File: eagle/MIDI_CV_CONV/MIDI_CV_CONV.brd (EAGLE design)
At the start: 94 x 71.1 mm, 37 parts, among them CN1 PWR9V, IC1 MCP4922, IC2 TLP552, IC3 74HC541N, IC4 TD62003

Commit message: Finish Soldering
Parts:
- moved R5 18.0 mm to (66.0, 63.5)
- moved R6 10.2 mm to (57.1, 66.0)
- moved JP1 5.39 mm to (8.89, 43.2), turned to 0 degrees
- moved C4 5.08 mm to (66.0, 11.4)
- moved CN1 2.54 mm to (36.8, 63.5)
- moved JP8 2.54 mm to (26.7, 38.1)
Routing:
- net +5V: track 290.4 -> 240.4 mm, vias 0 -> 2
- net N$26: track 46.3 -> 27.5 mm
- net N$1: track 12.7 -> 10.2 mm
- net N$2: track 53.3 -> 55.9 mm
- net +9V: track 10.2 -> 7.62 mm
- net N$24: track 3.61 -> 5.09 mm
- net N$3: track 17.3 -> 16.3 mm
- net GND: vias 2 -> 0

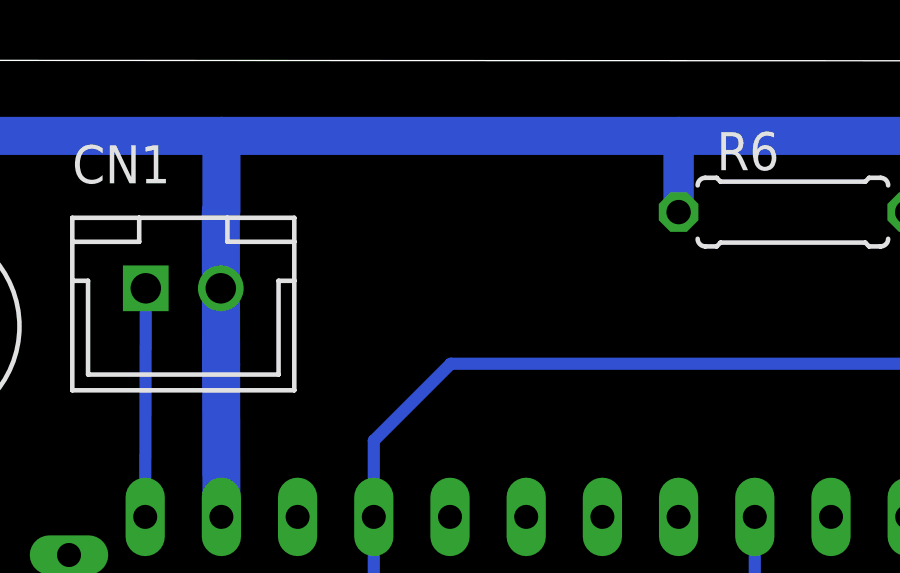
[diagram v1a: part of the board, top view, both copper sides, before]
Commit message: Add: 5V Power Supply
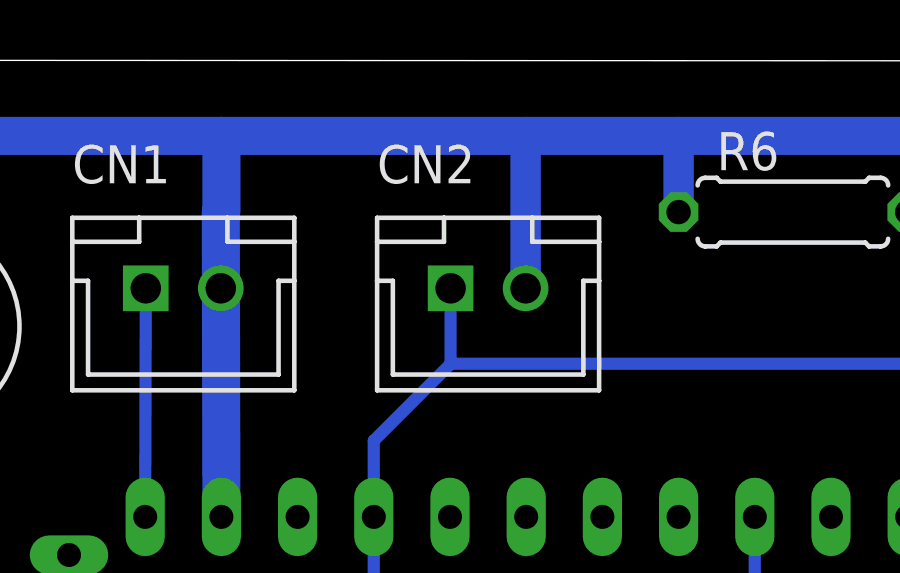
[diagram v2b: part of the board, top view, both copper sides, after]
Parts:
- added CN2: PWR5V, jst-xh:B2B-XH-A
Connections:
- net +5V: now also CN2.1
- net GND: now also CN2.2
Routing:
- net GND: track 298.4 -> 303.5 mm
- net +5V: track 240.4 -> 243.0 mm
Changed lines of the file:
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@@
 <element name="U$1" library="Arduino-clone" package="PRO-MINI-2" value="PRO-MINI-2 (16MHz/5V)" x="48.26" y="49.53" rot="R90"/>
 <element name="JP6" library="pinhead" library_urn="urn:adsk.eagle:library:325" package="1X01" package3d_urn="urn:adsk.eagle:package:22485/2" value="TP_CHK" x="68.58" y="43.18"/>
+<element name="CN2" library="jst-xh" package="B2B-XH-A" value="PWR5V" x="46.99" y="63.5"/>
 </elements>
 <signals>
@@
 <wire x1="10.16" y1="60.96" x2="5.08" y2="55.88" width="0.4064" layer="16"/>
 <wire x1="27.94" y1="60.96" x2="27.94" y2="53.34" width="0.4064" layer="16"/>
+<contactref element="CN2" pad="1"/>
+<wire x1="45.74" y1="63.5" x2="45.74" y2="60.9908" width="0.4064" layer="16"/>
+<wire x1="45.74" y1="60.9908" x2="45.7454" y2="60.9854" width="0.4064" layer="16"/>
 </signal>
 <signal name="N$4">
@@
 <wire x1="27.94" y1="63.5" x2="27.94" y2="68.58" width="1.27" layer="16"/>
 <wire x1="73.66" y1="68.58" x2="53.34" y2="68.58" width="1.27" layer="16"/>
-<wire x1="53.34" y1="68.58" x2="38.1" y2="68.58" width="1.27" layer="16"/>
+<wire x1="53.34" y1="68.58" x2="48.26" y2="68.58" width="1.27" layer="16"/>
+<wire x1="48.26" y1="68.58" x2="38.1" y2="68.58" width="1.27" layer="16"/>
 <wire x1="38.1" y1="12.7" x2="38.1" y2="17.78" width="1.27" layer="16"/>
 <wire x1="38.1" y1="17.78" x2="35.56" y2="20.32" width="1.27" layer="16"/>
@@
 <wire x1="66.04" y1="12.7" x2="63.5" y2="12.7" width="1.016" layer="16"/>
 <wire x1="76.2" y1="12.7" x2="66.04" y2="12.7" width="1.016" layer="16"/>
+<contactref element="CN2" pad="2"/>
+<wire x1="48.24" y1="63.5" x2="48.24" y2="68.56" width="1.016" layer="16"/>
+<wire x1="48.24" y1="68.56" x2="48.26" y2="68.58" width="1.016" layer="16"/>
 </signal>
 <signal name="N$5">
